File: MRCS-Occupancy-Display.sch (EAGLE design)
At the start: 4 parts

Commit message: early noodling on thru hole design
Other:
- note added: "Seth Neumann, Allison Dendy"
- note removed: "Your Name"
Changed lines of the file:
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@@
 <text x="240.03" y="12.7" size="2.1844" layer="97">1.0</text>
 <text x="241.3" y="6.35" size="2.1844" layer="97">A</text>
-<text x="166.37" y="6.35" size="2.1844" layer="97">Your Name</text>
+<text x="166.37" y="6.35" size="2.1844" layer="97">Seth Neumann, Allison Dendy</text>
 </plain>
 <instances>

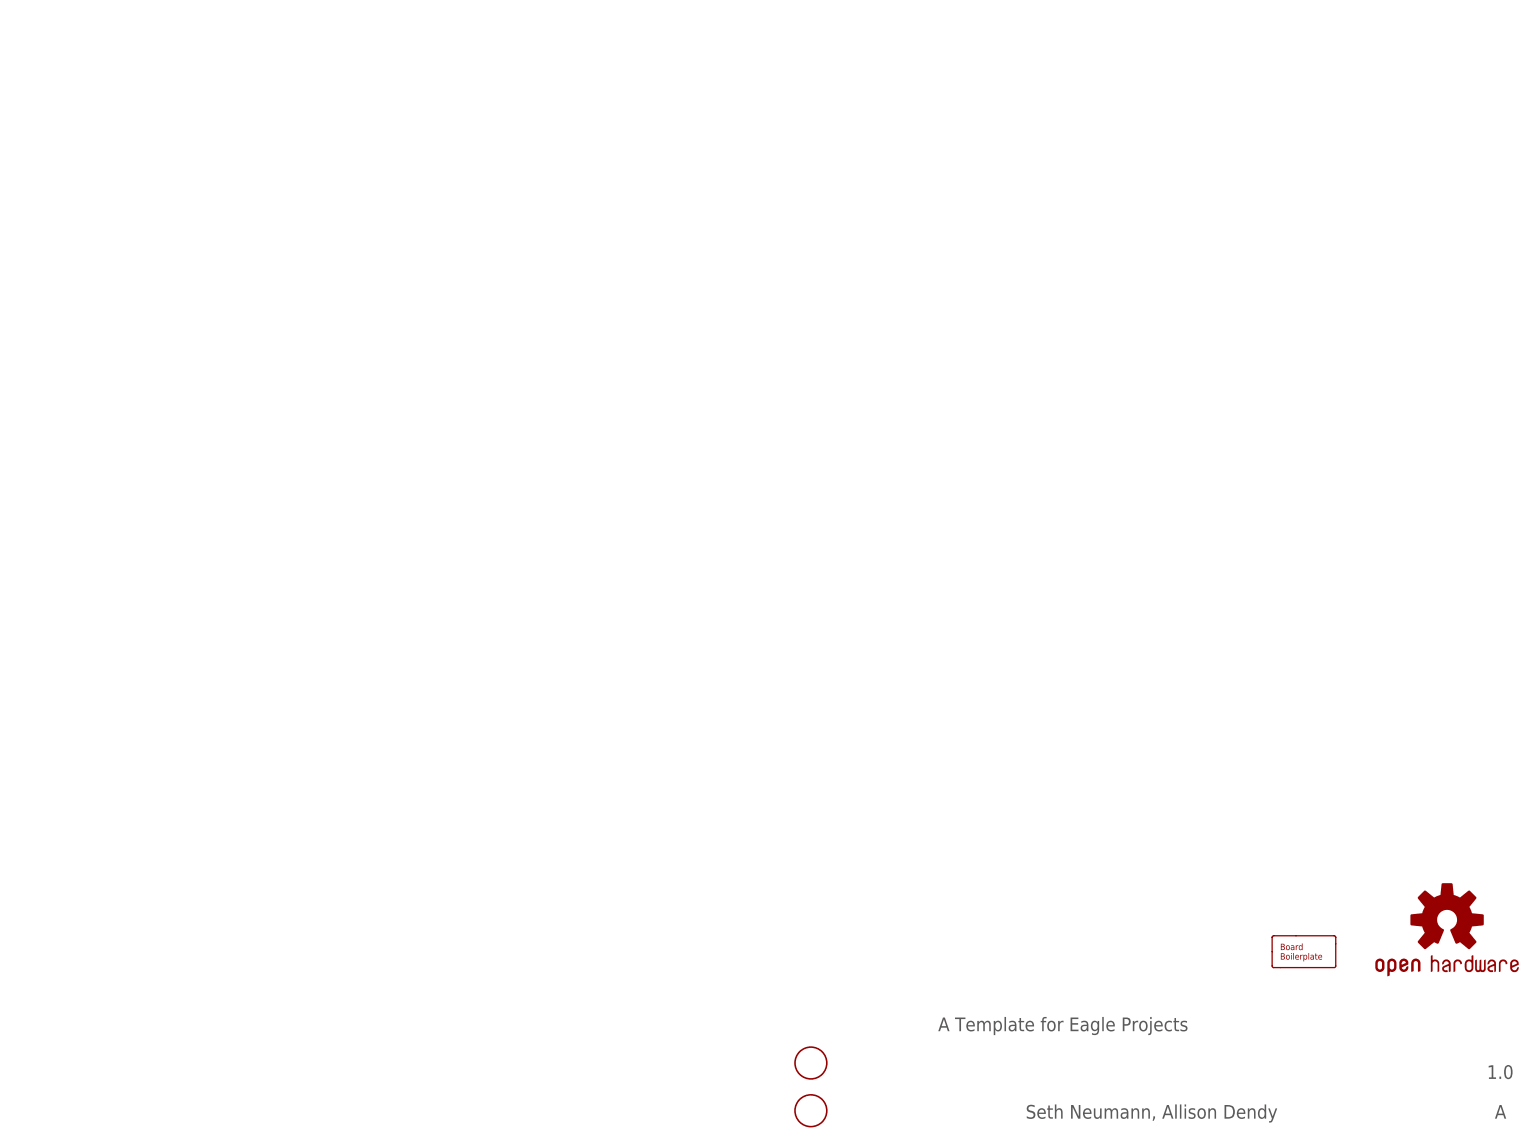
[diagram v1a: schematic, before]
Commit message: first pass of V1.0
basic 5x7 CM board per Allison
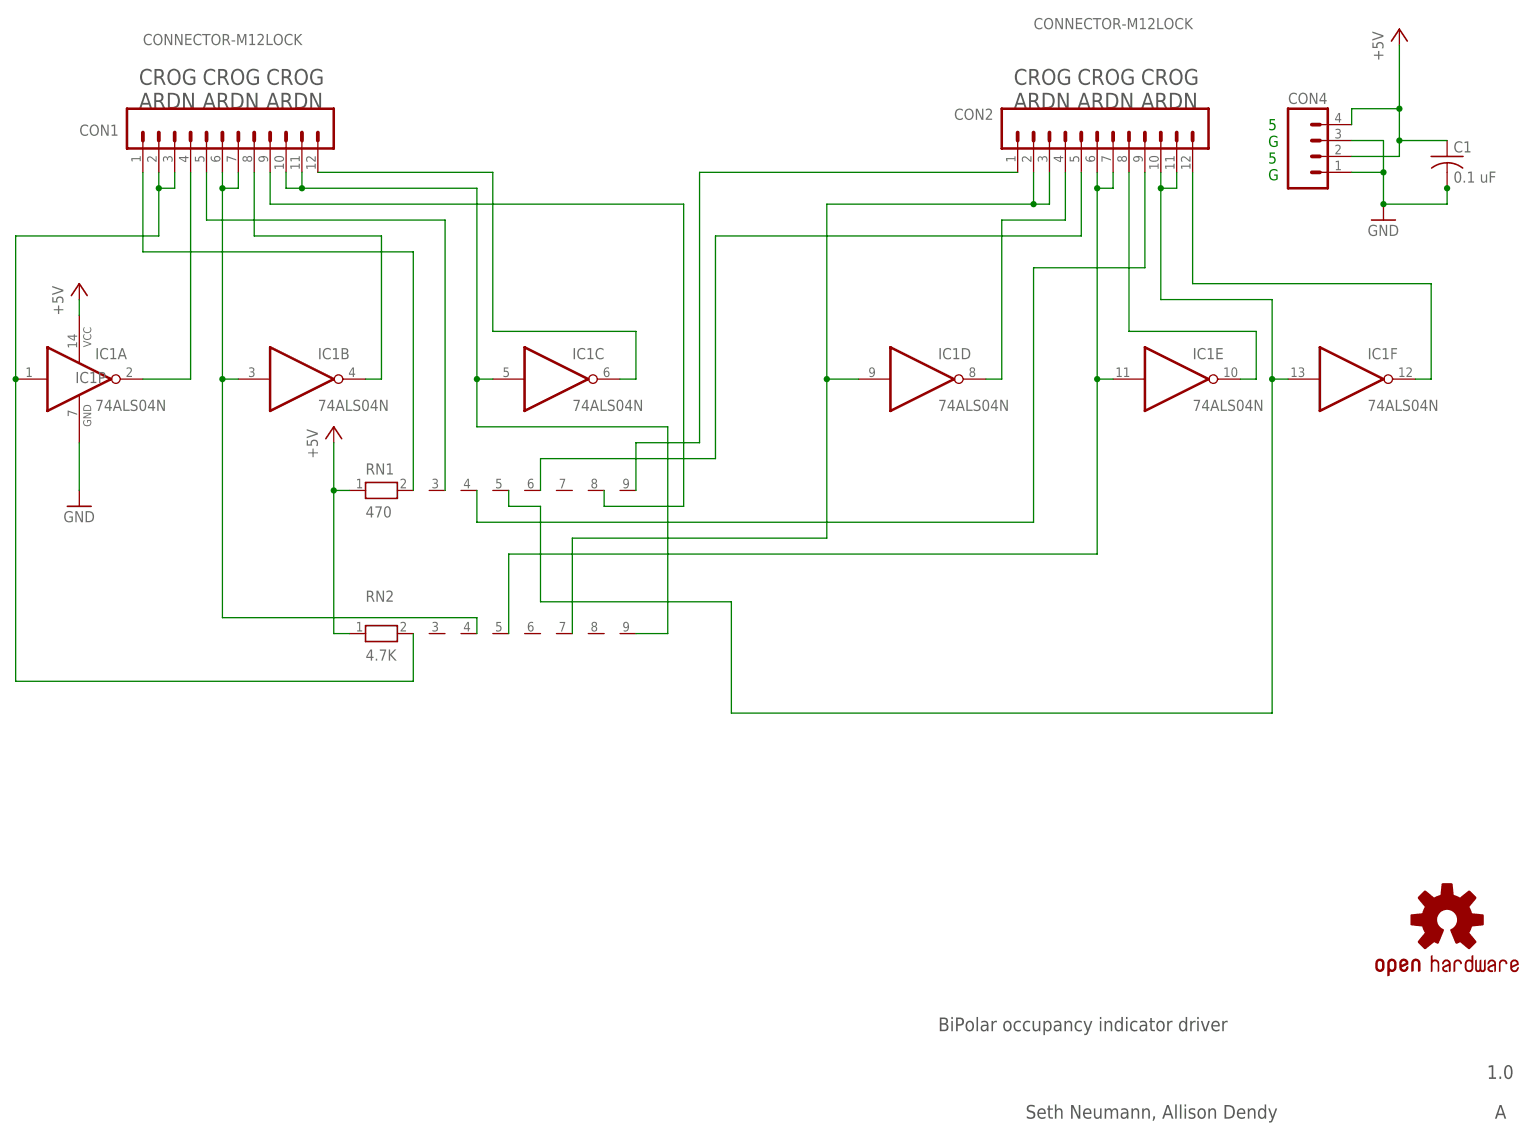
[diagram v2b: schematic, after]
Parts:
- removed BOARD1: BOARD80X100, SPCoast:BOARD80X100
- removed FID1, FID2: FIDUCIAL, SPCoast:FIDUCIAL
- added C1: 0.1 uF, SPCoast:CAPPTH2
- added CON1, CON2: CONNECTOR-M12LOCK, SPCoast:CONNECTOR-M12LOCK
- added CON4: (no value), SPCoast:CONNECTOR-M04SCREW
- added IC1: 74ALS04N, 74xx-us:74ALS04N
- added RN1: 470, resistor-net:RN08
- added RN2: 4.7K, resistor-net:RN08
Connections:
- new net GND: C1.2, CON4.1, CON4.3, IC1P.GND
- new net N$1: CON1.2, CON1.3, IC1A.I, RN2.2
- new net N$10: CON1.9, RN1.8
- new net N$11: CON2.8, IC1E.O
- new net N$12: CON2.12, IC1F.O
- new net N$13: CON2.4, IC1D.O
- new net N$14: CON2.1, RN1.9
- new net N$15: CON2.5, RN1.6
- new net N$18: CON2.6, CON2.7, IC1E.I, RN2.5
- new net N$19: CON2.9, RN1.4
- new net N$2: CON1.10, CON1.11, IC1C.I, RN2.9
- new net N$20: CON2.10, CON2.11, IC1F.I, RN1.5
- new net N$3: CON1.1, RN1.2
- new net N$4: CON1.4, IC1A.O
- new net N$5: CON1.6, CON1.7, IC1B.I, RN2.4
- new net N$6: CON1.12, IC1C.O
- new net N$7: CON1.8, IC1B.O
- new net N$8: CON1.5, RN1.3
- new net N$9: CON2.2, CON2.3, IC1D.I, RN2.7
- new net VCC: C1.1, CON4.2, CON4.4, IC1P.VCC, RN1.1, RN2.1
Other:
- note added: "5 G 5 G"
- note added: "BiPolar occupancy indicator driver"
- note added: "CROG ARDN"
- note removed: "A Template for Eagle Projects"

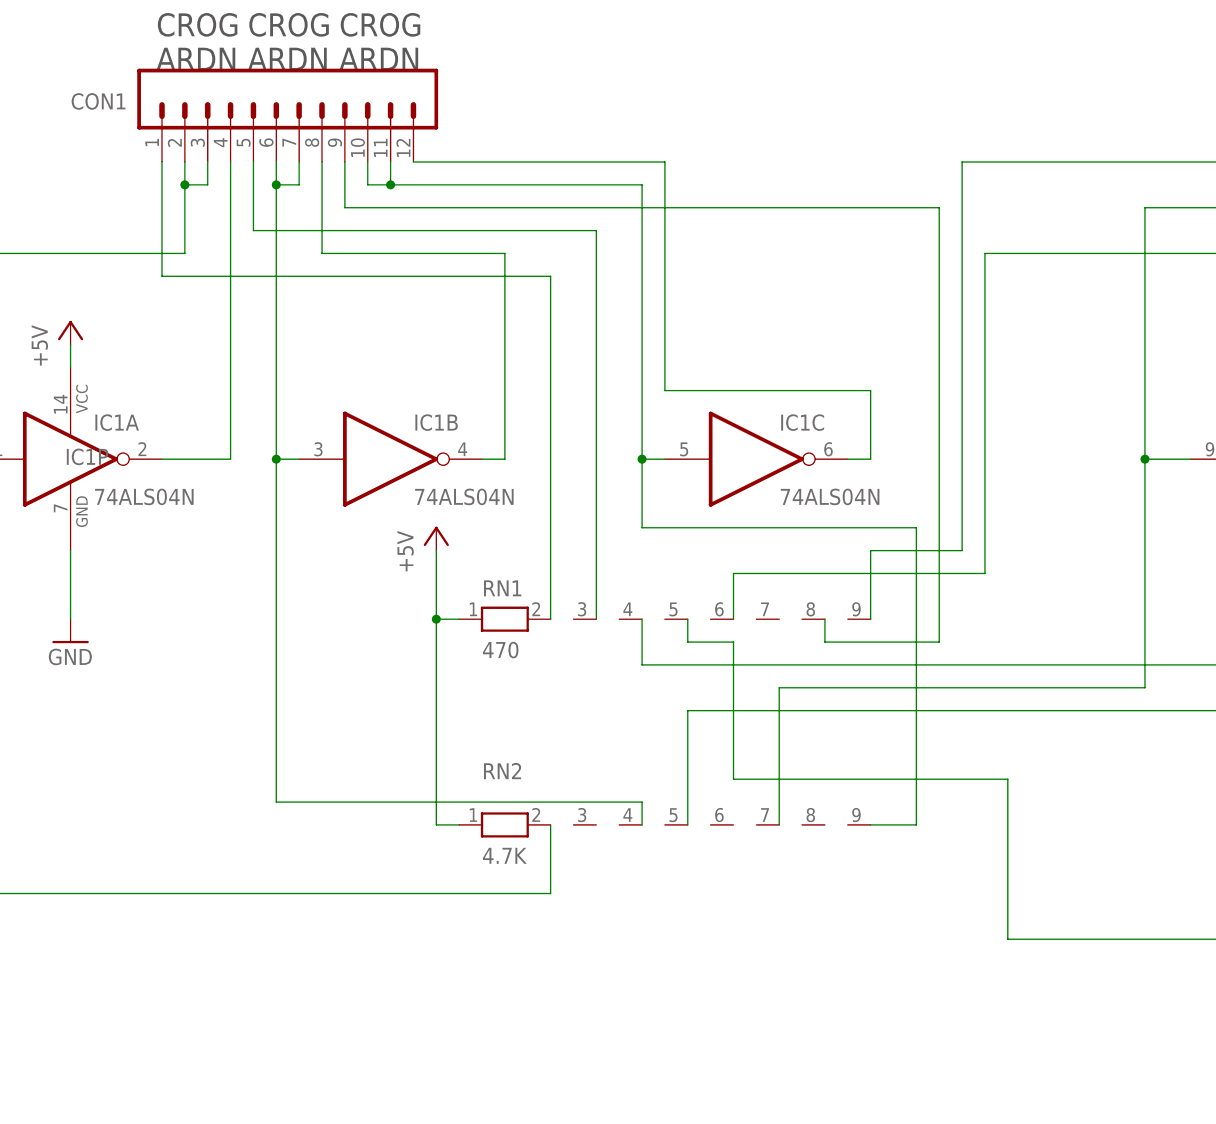
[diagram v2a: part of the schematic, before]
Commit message: modified the base design from 5x7 to 5x5 CM
The intent is to make a smaller footprint for panelization. It's pretty tight and not much room for labels.
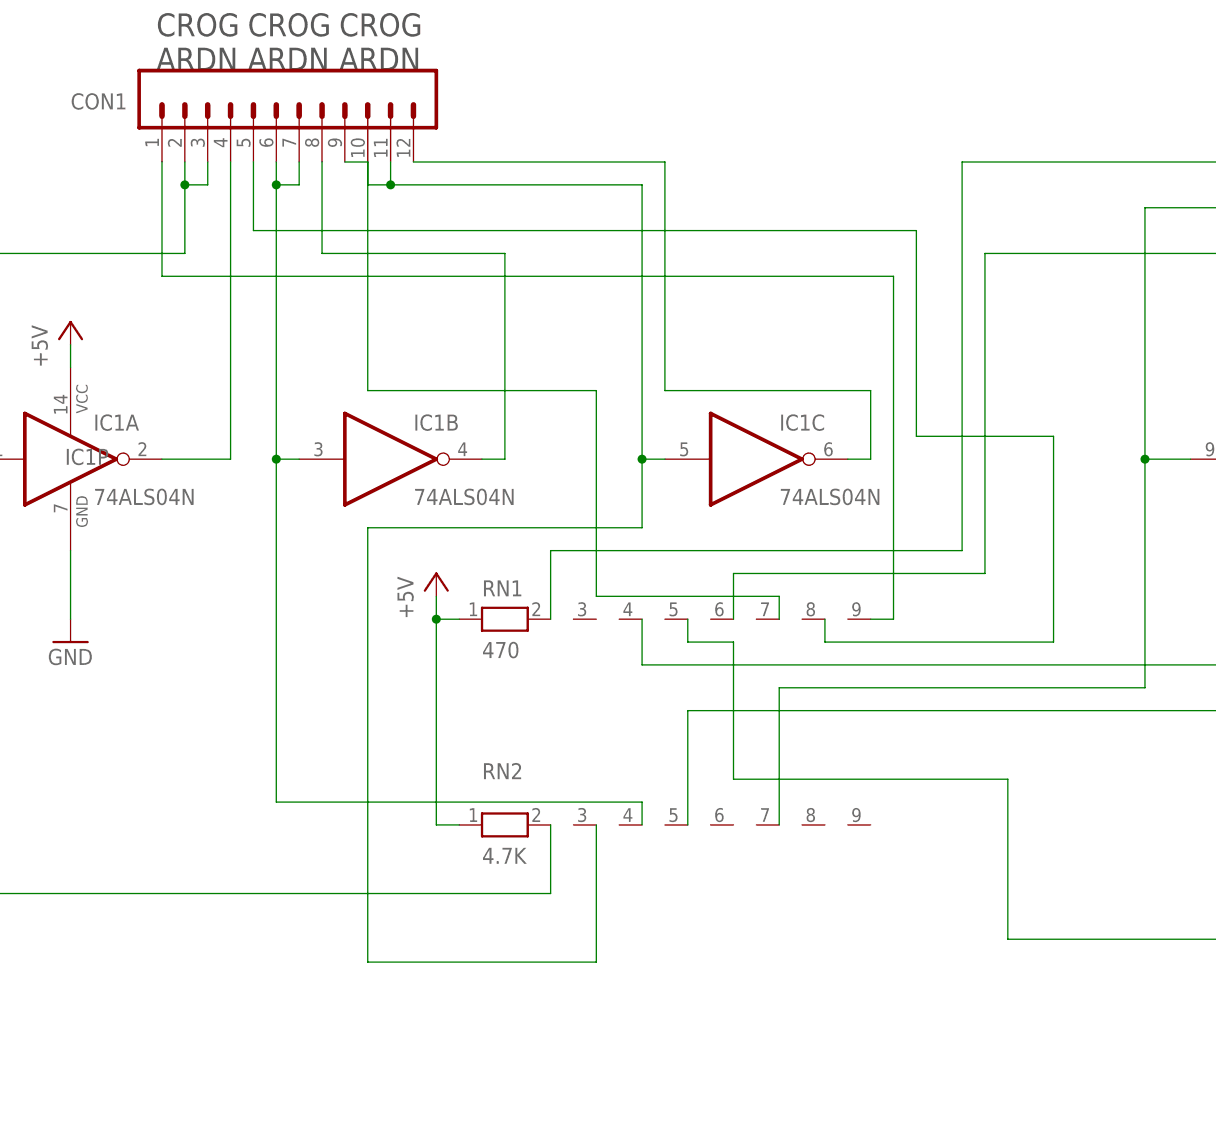
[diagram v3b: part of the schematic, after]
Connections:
- net N$10: now also RN1.7; no longer RN1.8
- net N$14: now also RN1.2; no longer RN1.9
- net N$2: now also RN2.3; no longer RN2.9
- net N$3: now also RN1.9; no longer RN1.2
- net N$8: now also RN1.8; no longer RN1.3
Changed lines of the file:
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@@
 <setting verticaltext="up"/>
 </settings>
-<grid distance="0.1" unitdist="inch" unit="inch" style="dots" multiple="1" display="yes" altdistance="25" altunitdist="mil" altunit="mil"/>
+<grid distance="100" unitdist="mil" unit="mil" style="dots" multiple="1" display="yes" altdistance="50" altunitdist="mil" altunit="mil"/>
 <layers>
 <layer number="1" name="Top" color="4" fill="1" visible="no" active="no"/>
@@
 <instance part="P+2" gate="1" x="15.24" y="139.7"/>
 <instance part="GND2" gate="1" x="15.24" y="104.14"/>
-<instance part="P+3" gate="1" x="55.88" y="116.84"/>
+<instance part="P+3" gate="1" x="55.88" y="111.76"/>
 <instance part="IC1" gate="A" x="15.24" y="124.46"/>
 <instance part="IC1" gate="B" x="50.8" y="124.46"/>
@@
 <segment>
 <pinref part="P+3" gate="1" pin="+5V"/>
-<wire x1="55.88" y1="114.3" x2="55.88" y2="106.68" width="0.4064" layer="91"/>
+<wire x1="55.88" y1="109.22" x2="55.88" y2="106.68" width="0.4064" layer="91"/>
 <pinref part="RN1" gate="1" pin="1"/>
 <wire x1="58.42" y1="106.68" x2="55.88" y2="106.68" width="0.4064" layer="91"/>
@@
 <net name="N$3" class="0">
 <segment>
-<pinref part="RN1" gate="1" pin="2"/>
-<wire x1="68.58" y1="106.68" x2="68.58" y2="144.78" width="0.4064" layer="91"/>
-<wire x1="68.58" y1="144.78" x2="25.4" y2="144.78" width="0.4064" layer="91"/>
 <pinref part="CON1" gate="G$1" pin="1"/>
-<wire x1="25.4" y1="144.78" x2="25.4" y2="157.48" width="0.4064" layer="91"/>
+<wire x1="25.4" y1="144.78" x2="25.4" y2="157.48" width="0.3048" layer="91"/>
+<wire x1="25.4" y1="144.78" x2="106.68" y2="144.78" width="0.3048" layer="91"/>
+<wire x1="106.68" y1="144.78" x2="106.68" y2="106.68" width="0.3048" layer="91"/>
+<pinref part="RN1" gate="1" pin="9"/>
+<wire x1="106.68" y1="106.68" x2="104.14" y2="106.68" width="0.3048" layer="91"/>
 </segment>
 </net>
@@
 <pinref part="CON1" gate="G$1" pin="5"/>
 <wire x1="35.56" y1="157.48" x2="35.56" y2="149.86" width="0.3048" layer="91"/>
-<wire x1="35.56" y1="149.86" x2="73.66" y2="149.86" width="0.3048" layer="91"/>
-<pinref part="RN1" gate="1" pin="3"/>
-<wire x1="73.66" y1="149.86" x2="73.66" y2="106.68" width="0.3048" layer="91"/>
+<wire x1="35.56" y1="149.86" x2="109.22" y2="149.86" width="0.3048" layer="91"/>
+<wire x1="109.22" y1="149.86" x2="109.22" y2="127" width="0.3048" layer="91"/>
+<wire x1="109.22" y1="127" x2="124.46" y2="127" width="0.3048" layer="91"/>
+<wire x1="124.46" y1="127" x2="124.46" y2="104.14" width="0.3048" layer="91"/>
+<wire x1="124.46" y1="104.14" x2="99.06" y2="104.14" width="0.3048" layer="91"/>
+<pinref part="RN1" gate="1" pin="8"/>
+<wire x1="99.06" y1="104.14" x2="99.06" y2="106.68" width="0.3048" layer="91"/>
 </segment>
 </net>
@@
 <wire x1="50.8" y1="157.48" x2="50.8" y2="154.94" width="0.3048" layer="91"/>
 <junction x="50.8" y="154.94"/>
-<wire x1="109.22" y1="116.84" x2="78.74" y2="116.84" width="0.3048" layer="91"/>
 <wire x1="78.74" y1="116.84" x2="78.74" y2="124.46" width="0.3048" layer="91"/>
 <junction x="78.74" y="124.46"/>
 <pinref part="IC1" gate="C" pin="I"/>
-<wire x1="109.22" y1="116.84" x2="109.22" y2="83.82" width="0.3048" layer="91"/>
-<pinref part="RN2" gate="1" pin="9"/>
-<wire x1="109.22" y1="83.82" x2="104.14" y2="83.82" width="0.3048" layer="91"/>
+<wire x1="78.74" y1="116.84" x2="48.26" y2="116.84" width="0.3048" layer="91"/>
+<wire x1="48.26" y1="116.84" x2="48.26" y2="68.58" width="0.3048" layer="91"/>
+<wire x1="48.26" y1="68.58" x2="73.66" y2="68.58" width="0.3048" layer="91"/>
+<pinref part="RN2" gate="1" pin="3"/>
+<wire x1="73.66" y1="68.58" x2="73.66" y2="83.82" width="0.3048" layer="91"/>
 </segment>
 </net>
@@
 <wire x1="104.14" y1="124.46" x2="101.6" y2="124.46" width="0.3048" layer="91"/>
 <pinref part="IC1" gate="C" pin="O"/>
-</segment>
-</net>
-<net name="N$10" class="0">
-<segment>
-<pinref part="CON1" gate="G$1" pin="9"/>
-<wire x1="45.72" y1="157.48" x2="45.72" y2="152.4" width="0.3048" layer="91"/>
-<wire x1="45.72" y1="152.4" x2="111.76" y2="152.4" width="0.3048" layer="91"/>
-<wire x1="111.76" y1="152.4" x2="111.76" y2="104.14" width="0.3048" layer="91"/>
-<wire x1="111.76" y1="104.14" x2="99.06" y2="104.14" width="0.3048" layer="91"/>
-<pinref part="RN1" gate="1" pin="8"/>
-<wire x1="99.06" y1="104.14" x2="99.06" y2="106.68" width="0.3048" layer="91"/>
 </segment>
 </net>
@@
 <wire x1="165.1" y1="157.48" x2="114.3" y2="157.48" width="0.3048" layer="91"/>
 <wire x1="114.3" y1="157.48" x2="114.3" y2="114.3" width="0.3048" layer="91"/>
-<wire x1="114.3" y1="114.3" x2="104.14" y2="114.3" width="0.3048" layer="91"/>
-<pinref part="RN1" gate="1" pin="9"/>
-<wire x1="104.14" y1="114.3" x2="104.14" y2="106.68" width="0.3048" layer="91"/>
+<wire x1="114.3" y1="114.3" x2="68.58" y2="114.3" width="0.3048" layer="91"/>
+<pinref part="RN1" gate="1" pin="2"/>
+<wire x1="68.58" y1="114.3" x2="68.58" y2="106.68" width="0.3048" layer="91"/>
 </segment>
 </net>
@@
 </segment>
 </net>
+<net name="N$10" class="0">
+<segment>
+<pinref part="CON1" gate="G$1" pin="9"/>
+<wire x1="45.72" y1="157.48" x2="48.26" y2="157.48" width="0.3048" layer="91"/>
+<wire x1="48.26" y1="157.48" x2="48.26" y2="132.08" width="0.3048" layer="91"/>
+<wire x1="48.26" y1="132.08" x2="73.66" y2="132.08" width="0.3048" layer="91"/>
+<wire x1="73.66" y1="132.08" x2="73.66" y2="109.22" width="0.3048" layer="91"/>
+<wire x1="73.66" y1="109.22" x2="93.98" y2="109.22" width="0.3048" layer="91"/>
+<pinref part="RN1" gate="1" pin="7"/>
+<wire x1="93.98" y1="109.22" x2="93.98" y2="106.68" width="0.3048" layer="91"/>
+</segment>
+</net>

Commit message: cleanup prior to putting product up on website
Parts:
- added C2: 0.1 uF, SPCoast:CAPPTH1
- added LED1: (no value), SPCoast:LEDLED3MM
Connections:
- removed net N$1: CON1.2, CON1.3, IC1A.I, RN2.2
- new net N$16: CON1.2, CON1.3, IC1A.I, RN2.3
- new net N$17: LED1.A, RN1.5
- net GND: now also C2.2, LED1.C
- net N$15: now also RN1.4; no longer RN1.6
- net N$18: now also RN2.7; no longer RN2.5
- net N$19: now also RN1.3; no longer RN1.4
- net N$2: now also RN2.2; no longer RN2.3
- net N$20: now also RN2.6; no longer RN1.5
- net N$9: now also RN2.9; no longer RN2.7
- net VCC: now also C2.1
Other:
- note added: "1.1"
- note added: "BiPolar occupancy indicator driver 4x4"
- note added: "CROG ADDN"
- note added: "Use 1 of C1, C2"
- note removed: "1.0"
- note removed: "BiPolar occupancy indicator driver"
- note removed: "CROG ARDN"
- moved on the sheet: RN2
